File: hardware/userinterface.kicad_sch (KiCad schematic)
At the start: 16 parts, among them J3 NHD-2.4-240320AF-CSXP, SW3 L-KLS4-EC1121S-E5A-F12.5, U7 TPS61023DRLR, U8 CAT4104V-GT3

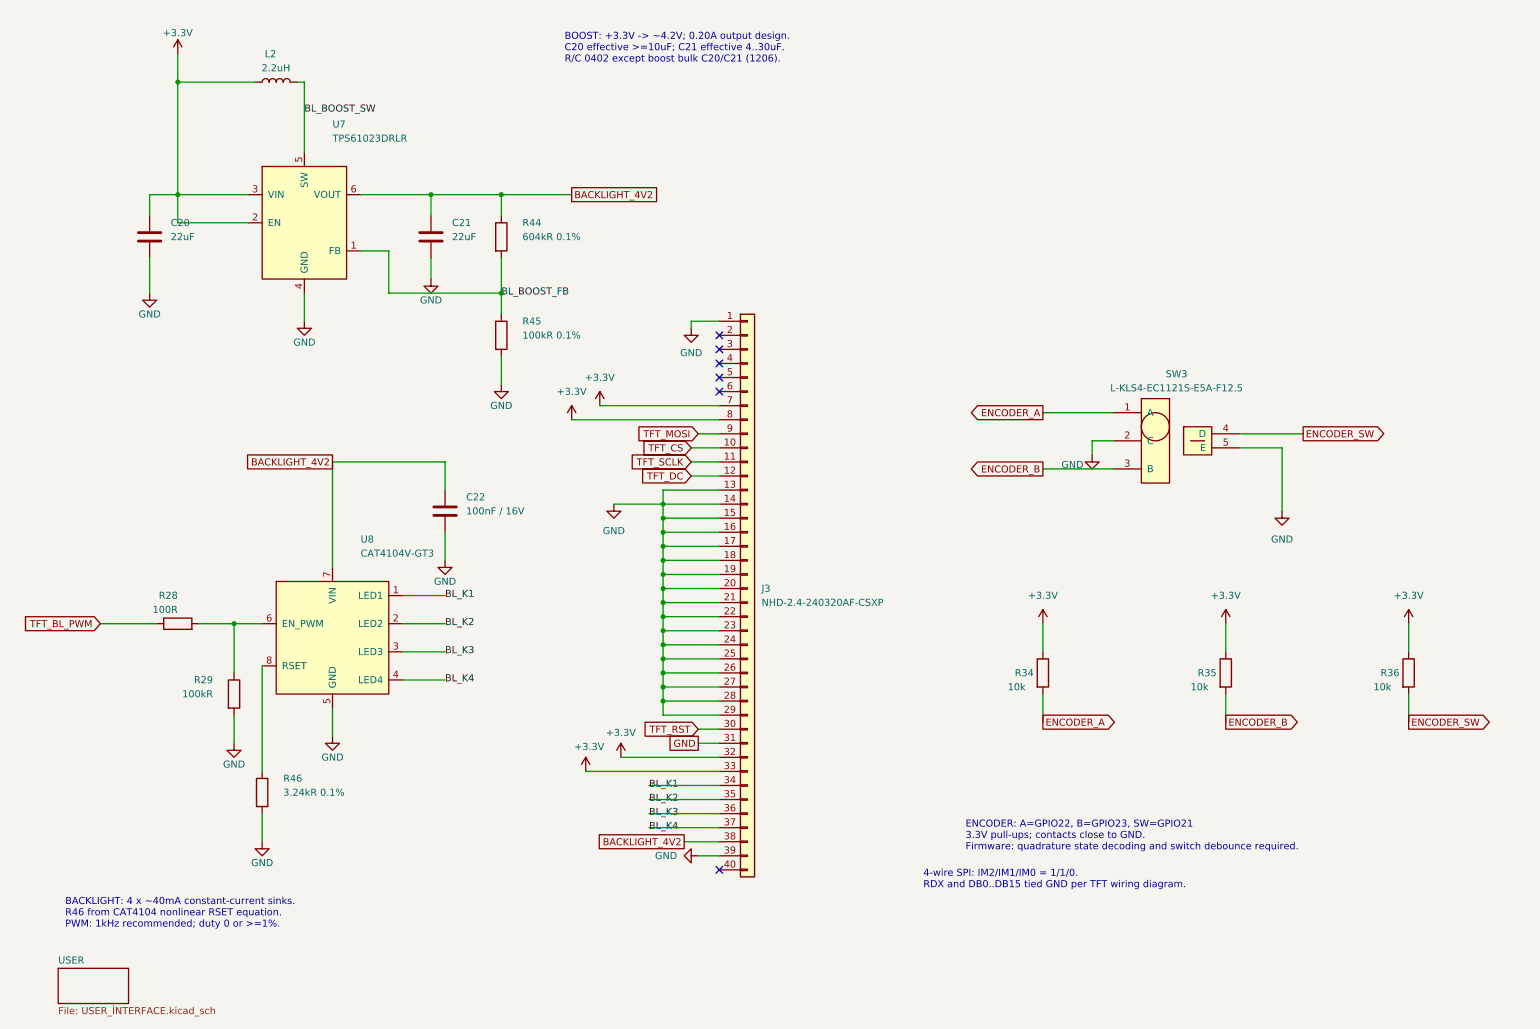
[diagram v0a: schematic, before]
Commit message: userinterface: sayfayı dört blok halinde yeniden çiz
TPS61023 boost, CAT4104 sürücü, TFT J3 ve enkoder ayrı çerçevelerde;
J3 GND pinleri tek barada, enkoder pull-up'ları kesişmesiz. Dirençler
R_Small_US. J3.31 GND global etiketi 2.54 mm aralık yüzünden korundu.
Netlist değişmedi.

Co-Authored-By: Claude Opus 5 <noreply@anthropic.com>
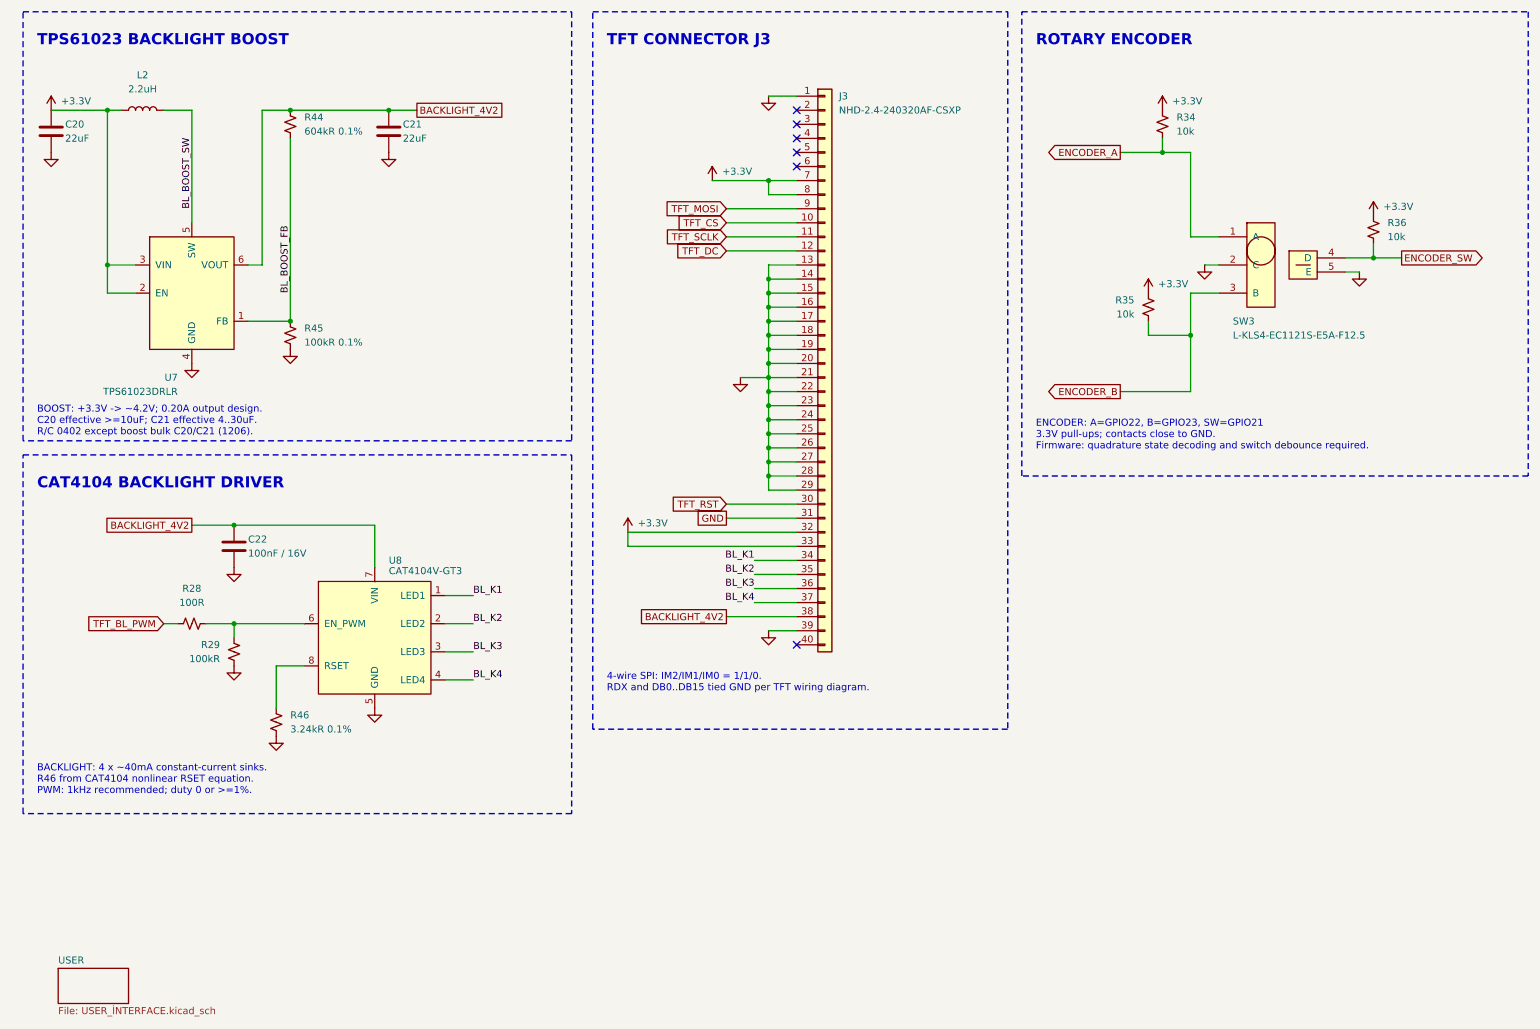
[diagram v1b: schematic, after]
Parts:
- R28, R29, R34, R35, R36, R44, R45, R46: symbol Device:R -> Device:R_Small_US
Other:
- note added: "CAT4104 BACKLIGHT DRIVER"
- note added: "ROTARY ENCODER"
- note added: "TFT CONNECTOR J3"
- note added: "TPS61023 BACKLIGHT BOOST"
- moved on the sheet: C20, C21, C22, J3, L2, SW3, U7, U8
